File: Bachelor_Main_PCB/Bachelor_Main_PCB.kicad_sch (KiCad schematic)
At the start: 4 parts

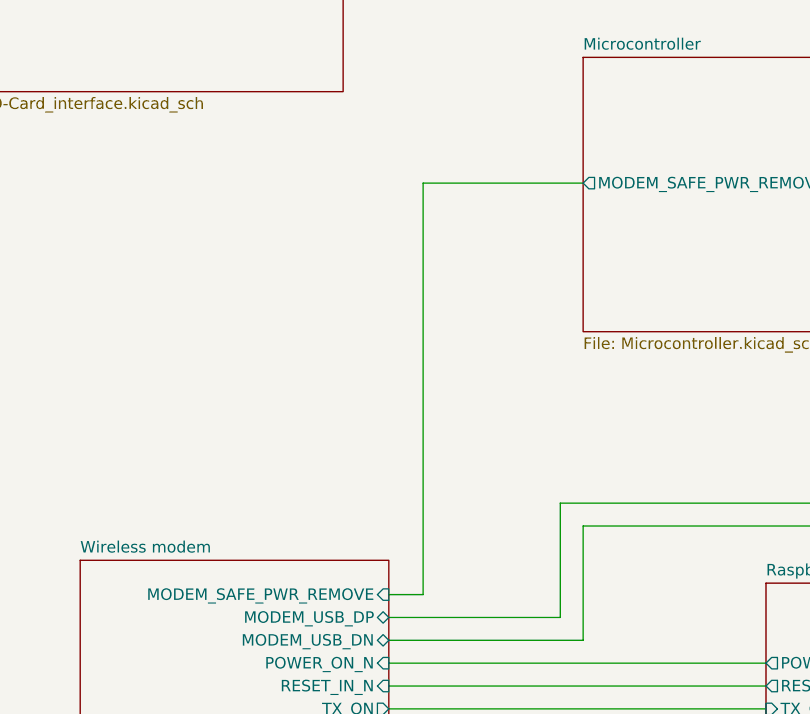
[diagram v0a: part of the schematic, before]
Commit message: Updated TVS diode routing through N/C pins
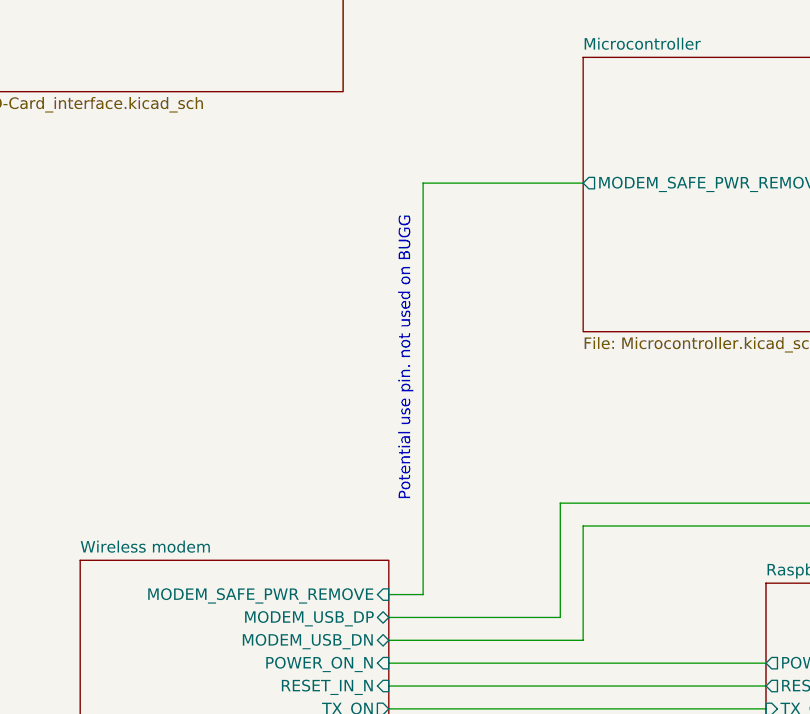
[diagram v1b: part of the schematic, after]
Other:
- note added: "Potential use pin. not used on BUGG"
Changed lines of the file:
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@@
+		)
+	)
+	(text "Potential use pin. not used on BUGG"
+		(exclude_from_sim no)
+		(at 81.788 80.518 90)
+		(effects
+			(font
+				(size 1.27 1.27)
+			)
 		)
 	)

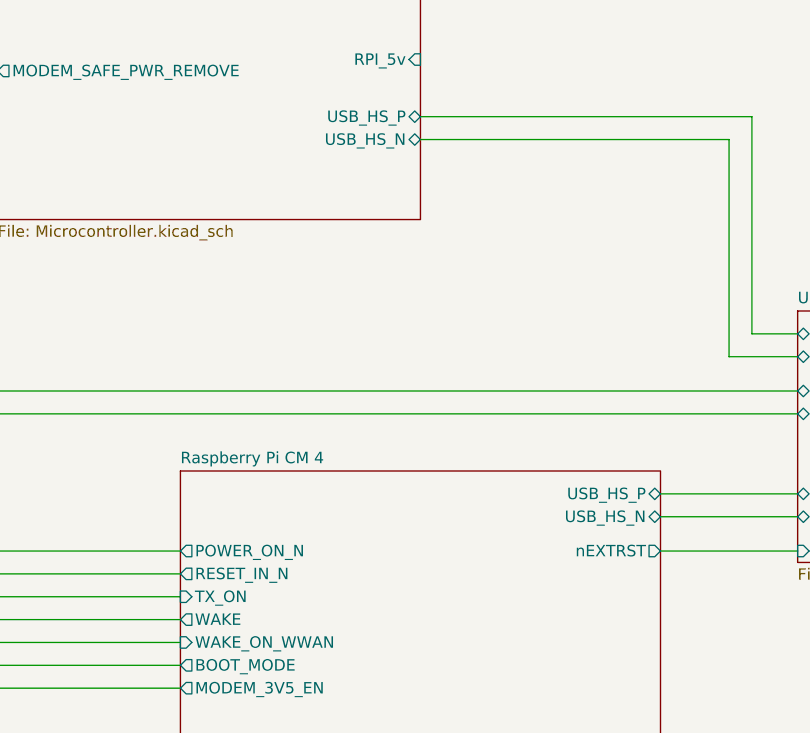
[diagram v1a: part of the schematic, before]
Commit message: Add RPI to MCU UART communication
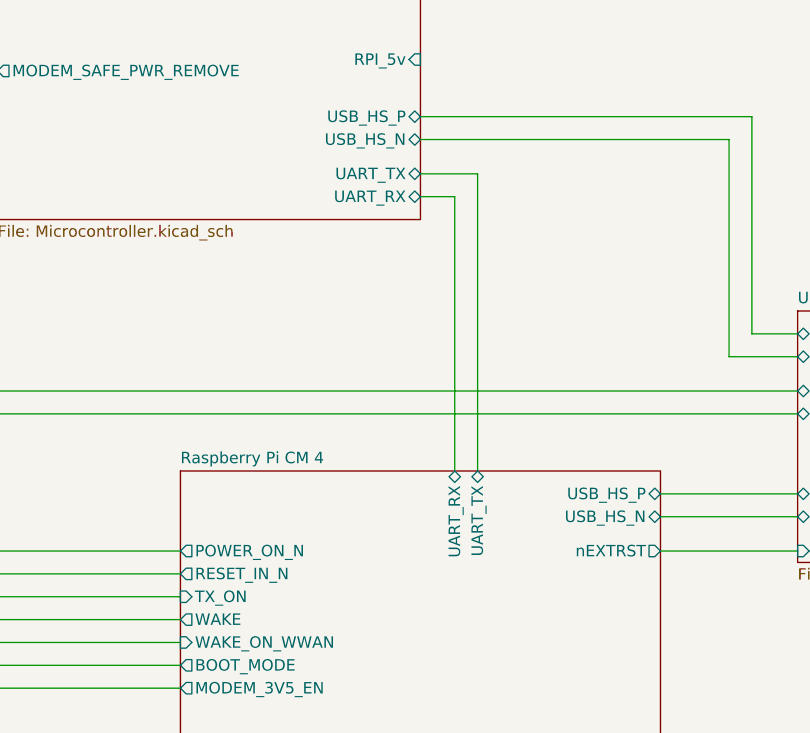
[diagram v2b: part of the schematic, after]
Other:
- sheet Microcontroller ports: added UART_RX, UART_TX; removed none
- sheet Raspberry Pi CM 4 ports: added UART_RX, UART_TX; removed none
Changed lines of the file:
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@@
+	(wire
+		(pts
+			(xy 152.4 74.93) (xy 152.4 105.41)
+		)
+		(stroke
+			(width 0)
+			(type default)
+		)
+	)
 	(wire
 		(pts
@@
 	(wire
 		(pts
+			(xy 154.94 105.41) (xy 154.94 72.39)
+		)
+		(stroke
+			(width 0)
+			(type default)
+		)
+	)
+	(wire
+		(pts
 			(xy 83.82 60.96) (xy 101.6 60.96)
 		)
@@
 	(wire
 		(pts
+			(xy 154.94 72.39) (xy 148.59 72.39)
+		)
+		(stroke
+			(width 0)
+			(type default)
+		)
+	)
+	(wire
+		(pts
 			(xy 83.82 106.68) (xy 83.82 60.96)
 		)
@@
 		(pts
 			(xy 80.01 121.92) (xy 121.92 121.92)
+		)
+		(stroke
+			(width 0)
+			(type default)
+		)
+	)
+	(wire
+		(pts
+			(xy 148.59 74.93) (xy 152.4 74.93)
 		)
 		(stroke
@@
 			)
 		)
+		(pin "UART_RX" bidirectional
+			(at 152.4 105.41 90)
+			(effects
+				(font
+					(size 1.27 1.27)
+				)
+				(justify right)
+			)
+		)
+		(pin "UART_TX" bidirectional
+			(at 154.94 105.41 90)
+			(effects
+				(font
+					(size 1.27 1.27)
+				)
+				(justify right)
+			)
+		)
 		(instances
 			(project "Bachelor_Main_PCB"
@@
 			)
 		)
+		(pin "UART_RX" bidirectional
+			(at 148.59 74.93 0)
+			(effects
+				(font
+					(size 1.27 1.27)
+				)
+				(justify right)
+			)
+		)
+		(pin "UART_TX" bidirectional
+			(at 148.59 72.39 0)
+			(effects
+				(font
+					(size 1.27 1.27)
+				)
+				(justify right)
+			)
+		)

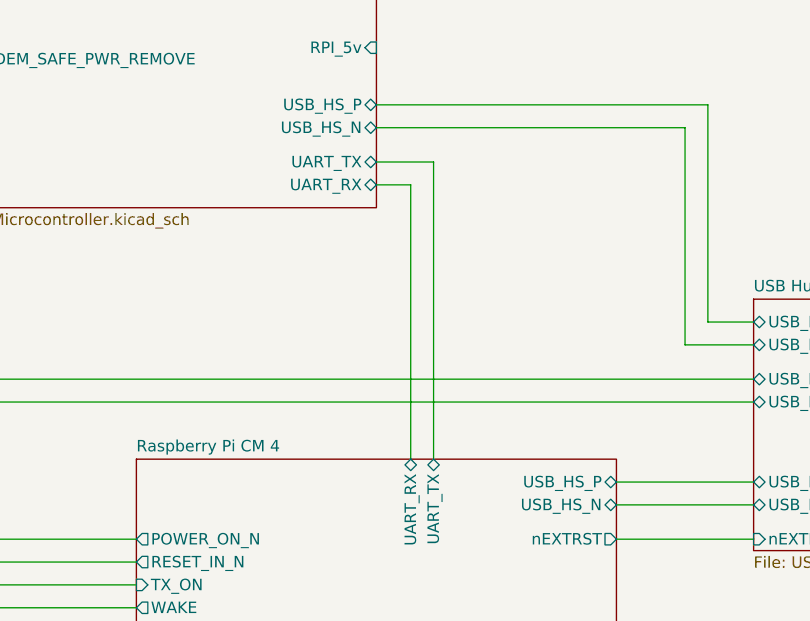
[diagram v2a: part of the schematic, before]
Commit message: Switched RX and TX for UART connection
so that the TX from RPI go into RX on MCU
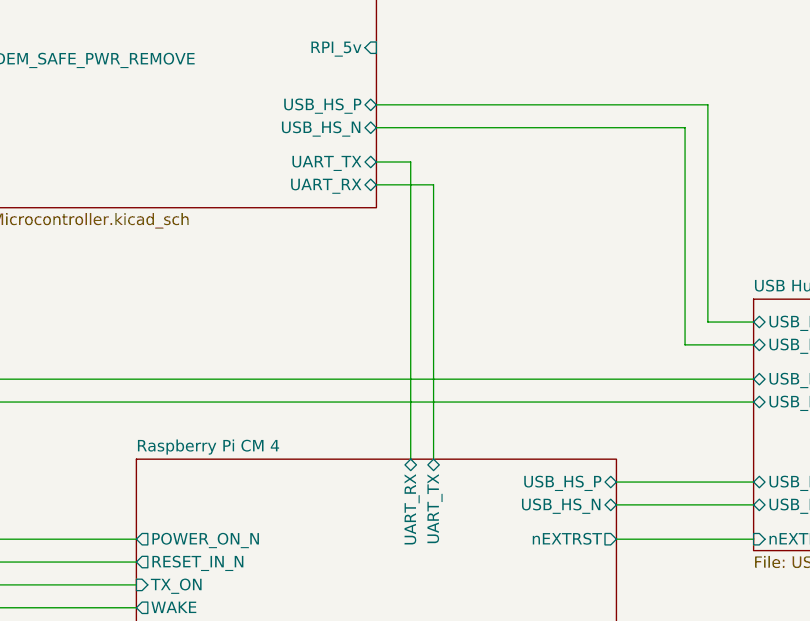
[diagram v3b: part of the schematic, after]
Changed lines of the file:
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@@
 	(wire
 		(pts
-			(xy 152.4 74.93) (xy 152.4 105.41)
+			(xy 152.4 72.39) (xy 152.4 105.41)
 		)
 		(stroke
@@
 	(wire
 		(pts
-			(xy 154.94 105.41) (xy 154.94 72.39)
-		)
-		(stroke
-			(width 0)
-			(type default)
-		)
-	)
-	(wire
-		(pts
 			(xy 83.82 60.96) (xy 101.6 60.96)
 		)
@@
 	(wire
 		(pts
+			(xy 148.59 72.39) (xy 152.4 72.39)
+		)
+		(stroke
+			(width 0)
+			(type default)
+		)
+	)
+	(wire
+		(pts
 			(xy 99.06 96.52) (xy 99.06 109.22)
 		)
@@
 	(wire
 		(pts
+			(xy 148.59 74.93) (xy 154.94 74.93)
+		)
+		(stroke
+			(width 0)
+			(type default)
+		)
+	)
+	(wire
+		(pts
 			(xy 185.42 66.04) (xy 148.59 66.04)
 		)
@@
 	(wire
 		(pts
-			(xy 154.94 72.39) (xy 148.59 72.39)
-		)
-		(stroke
-			(width 0)
-			(type default)
-		)
-	)
-	(wire
-		(pts
 			(xy 83.82 106.68) (xy 83.82 60.96)
 		)
@@
 	(wire
 		(pts
-			(xy 148.59 74.93) (xy 152.4 74.93)
-		)
-		(stroke
-			(width 0)
-			(type default)
-		)
-	)
-	(wire
-		(pts
 			(xy 80.01 119.38) (xy 121.92 119.38)
 		)
 		(stroke
+			(width 0)
+			(type default)
+		)
+	)
+	(wire
+		(pts
+			(xy 154.94 74.93) (xy 154.94 105.41)
+		)
+		(stroke

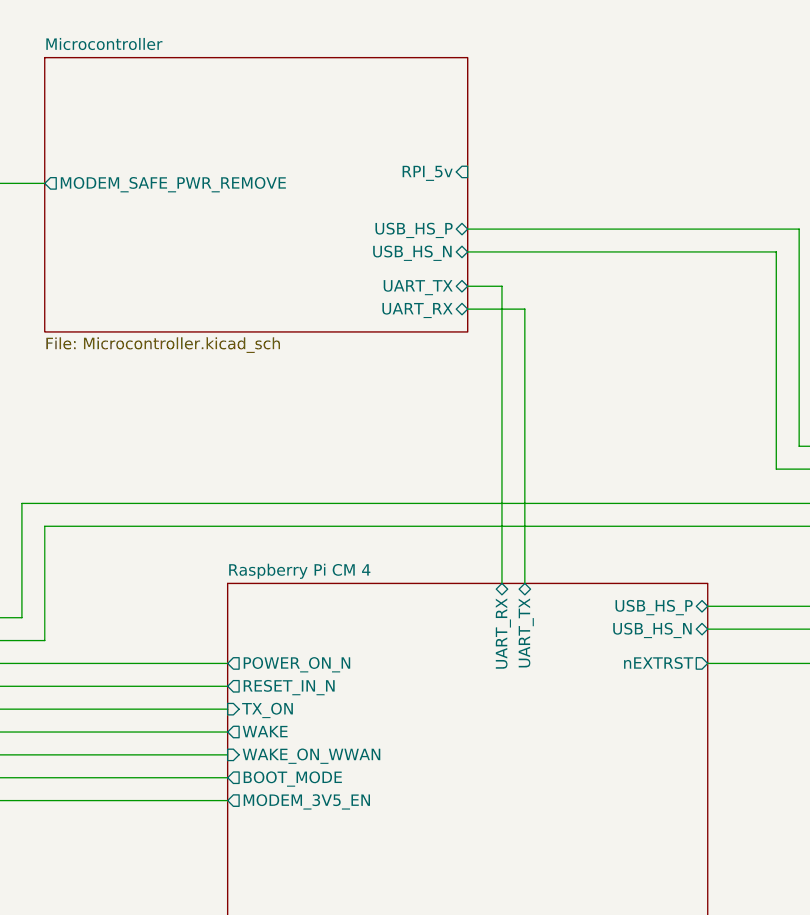
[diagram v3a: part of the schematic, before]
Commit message: Add RPI CM enable pin to MCU sheet
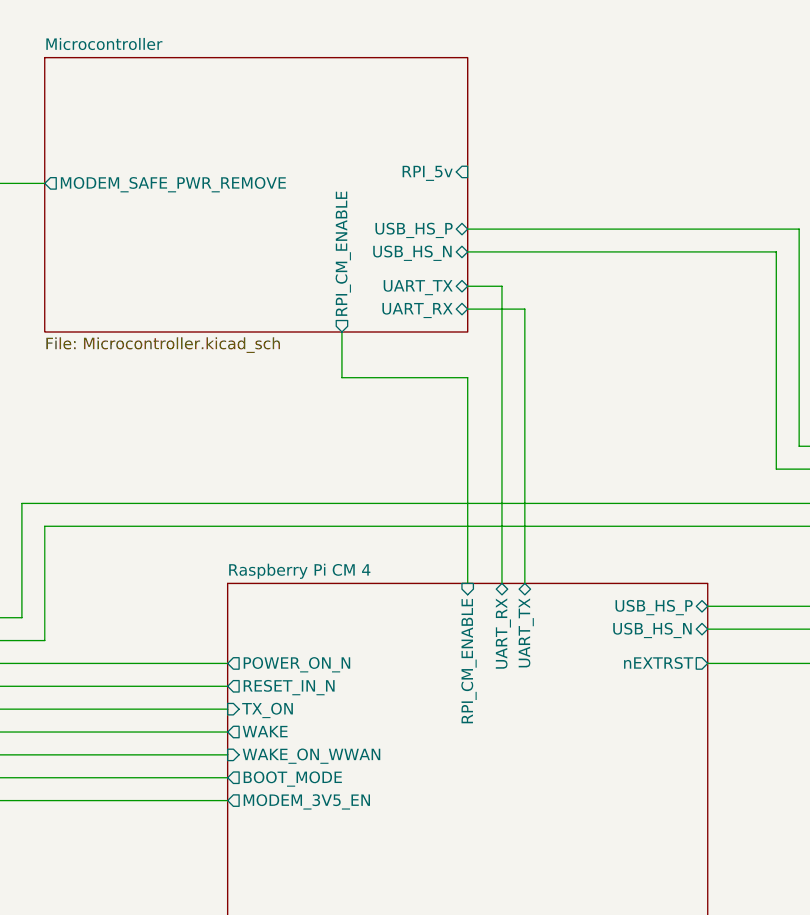
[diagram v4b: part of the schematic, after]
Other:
- sheet Microcontroller ports: added RPI_CM_ENABLE; removed none
- sheet Raspberry Pi CM 4 ports: added RPI_CM_ENABLE; removed none
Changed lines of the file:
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@@
+	(wire
+		(pts
+			(xy 148.59 105.41) (xy 148.59 82.55)
+		)
+		(stroke
+			(width 0)
+			(type default)
+		)
+	)
 	(wire
 		(pts
@@
 		(pts
 			(xy 80.01 121.92) (xy 121.92 121.92)
+		)
+		(stroke
+			(width 0)
+			(type default)
+		)
+	)
+	(wire
+		(pts
+			(xy 148.59 82.55) (xy 134.62 82.55)
+		)
+		(stroke
+			(width 0)
+			(type default)
+		)
+	)
+	(wire
+		(pts
+			(xy 134.62 82.55) (xy 134.62 77.47)
 		)
 		(stroke
@@
 			)
 		)
+		(pin "RPI_CM_ENABLE" input
+			(at 148.59 105.41 90)
+			(effects
+				(font
+					(size 1.27 1.27)
+				)
+				(justify right)
+			)
+		)
 		(instances
 			(project "Bachelor_Main_PCB"
@@
 			)
 		)
+		(pin "RPI_CM_ENABLE" output
+			(at 134.62 77.47 270)
+			(effects
+				(font
+					(size 1.27 1.27)
+				)
+				(justify left)
+			)
+		)

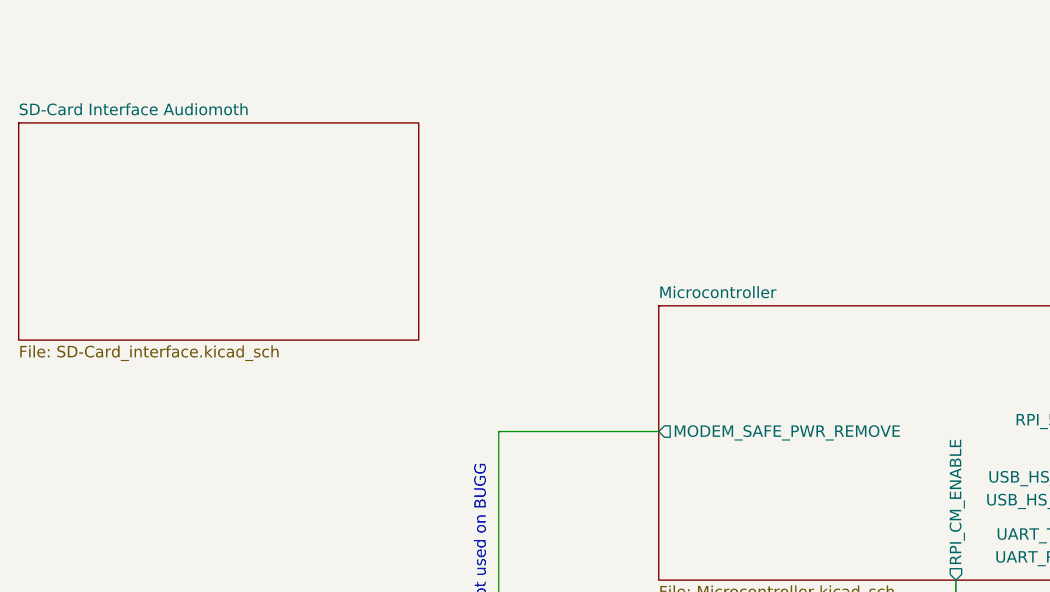
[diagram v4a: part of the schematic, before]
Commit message: Add audiomoth to MCU SPI
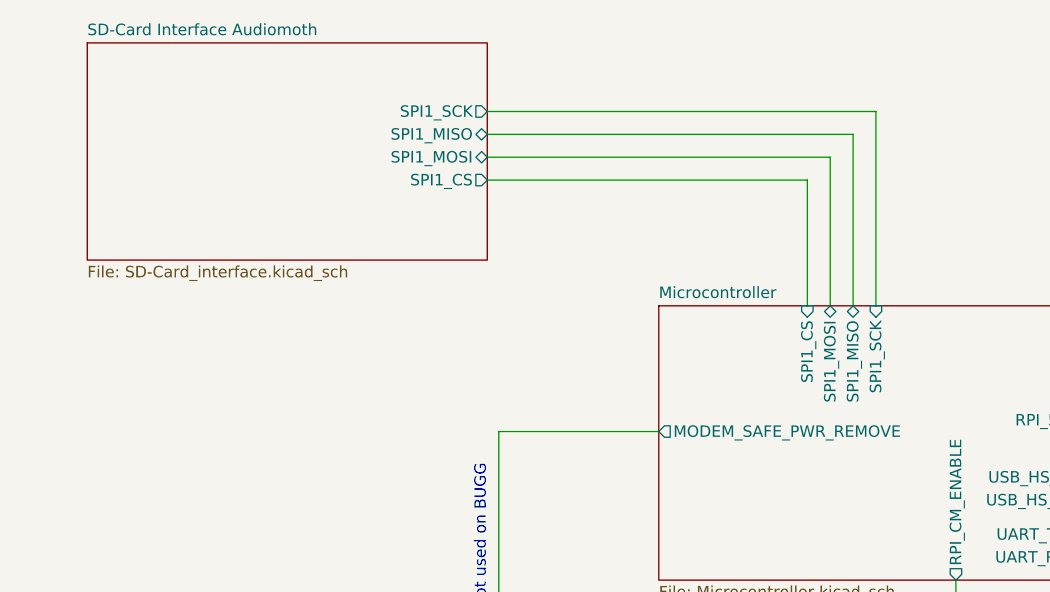
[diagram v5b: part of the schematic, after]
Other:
- sheet Microcontroller ports: added SPI1_CS, SPI1_MISO, SPI1_MOSI, SPI1_SCK; removed none
- sheet SD-Card Interface Audiomoth ports: added SPI1_CS, SPI1_MISO, SPI1_MOSI, SPI1_SCK; removed none
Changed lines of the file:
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@@
+	(wire
+		(pts
+			(xy 118.11 33.02) (xy 118.11 46.99)
+		)
+		(stroke
+			(width 0)
+			(type default)
+		)
+	)
 	(wire
 		(pts
@@
 	(wire
 		(pts
+			(xy 123.19 27.94) (xy 123.19 46.99)
+		)
+		(stroke
+			(width 0)
+			(type default)
+		)
+	)
+	(wire
+		(pts
 			(xy 80.01 111.76) (xy 101.6 111.76)
 		)
@@
 	(wire
 		(pts
+			(xy 120.65 30.48) (xy 82.55 30.48)
+		)
+		(stroke
+			(width 0)
+			(type default)
+		)
+	)
+	(wire
+		(pts
 			(xy 182.88 68.58) (xy 148.59 68.58)
 		)
@@
 	(wire
 		(pts
+			(xy 125.73 25.4) (xy 82.55 25.4)
+		)
+		(stroke
+			(width 0)
+			(type default)
+		)
+	)
+	(wire
+		(pts
+			(xy 125.73 46.99) (xy 125.73 25.4)
+		)
+		(stroke
+			(width 0)
+			(type default)
+		)
+	)
+	(wire
+		(pts
+			(xy 82.55 27.94) (xy 123.19 27.94)
+		)
+		(stroke
+			(width 0)
+			(type default)
+		)
+	)
+	(wire
+		(pts
 			(xy 83.82 60.96) (xy 101.6 60.96)
 		)
@@
 	(wire
 		(pts
+			(xy 82.55 33.02) (xy 118.11 33.02)
+		)
+		(stroke
+			(width 0)
+			(type default)
+		)
+	)
+	(wire
+		(pts
 			(xy 148.59 72.39) (xy 152.4 72.39)
 		)
@@
 		(pts
 			(xy 185.42 66.04) (xy 148.59 66.04)
+		)
+		(stroke
+			(width 0)
+			(type default)
+		)
+	)
+	(wire
+		(pts
+			(xy 120.65 46.99) (xy 120.65 30.48)
 		)
 		(stroke
@@
 			)
 		)
+		(pin "SPI1_CS" input
+			(at 118.11 46.99 90)
+			(effects
+				(font
+					(size 1.27 1.27)
+				)
+				(justify right)
+			)
+		)
+		(pin "SPI1_MISO" bidirectional
+			(at 123.19 46.99 90)
+			(effects
+				(font
+					(size 1.27 1.27)
+				)
+				(justify right)
+			)
+		)
+		(pin "SPI1_MOSI" bidirectional
+			(at 120.65 46.99 90)
+			(effects
+				(font
+					(size 1.27 1.27)
+				)
+				(justify right)
+			)
+		)
+		(pin "SPI1_SCK" input
+			(at 125.73 46.99 90)
+			(effects
+				(font
+					(size 1.27 1.27)
+				)
+				(justify right)
+			)
+		)
 		(instances
 			(project "Bachelor_Main_PCB"
@@
 	)
 	(sheet
-		(at 30.48 26.67)
+		(at 38.1 17.78)
 		(size 44.45 24.13)
 		(exclude_from_sim no)
@@
 		)
 		(property "Sheetname" "SD-Card Interface Audiomoth"
-			(at 30.48 25.9584 0)
+			(at 38.1 17.0684 0)
 			(effects
 				(font
@@
 		)
 		(property "Sheetfile" "SD-Card_interface.kicad_sch"
-			(at 30.48 51.3846 0)
+			(at 38.1 42.4946 0)
 			(effects
 				(font
@@
 			)
 		)
+		(pin "SPI1_CS" output
+			(at 82.55 33.02 0)
+			(effects
+				(font
+					(size 1.27 1.27)
+				)
+				(justify right)
+			)
+		)
+		(pin "SPI1_MISO" bidirectional
+			(at 82.55 27.94 0)
+			(effects
+				(font
+					(size 1.27 1.27)
+				)
+				(justify right)
+			)
+		)
+		(pin "SPI1_MOSI" bidirectional
+			(at 82.55 30.48 0)
+			(effects
+				(font
+					(size 1.27 1.27)
+				)
+				(justify right)
+			)
+		)
+		(pin "SPI1_SCK" output
+			(at 82.55 25.4 0)
+			(effects
+				(font
+					(size 1.27 1.27)
+				)
+				(justify right)
+			)
+		)
